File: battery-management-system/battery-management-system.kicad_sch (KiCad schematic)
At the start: 0 parts

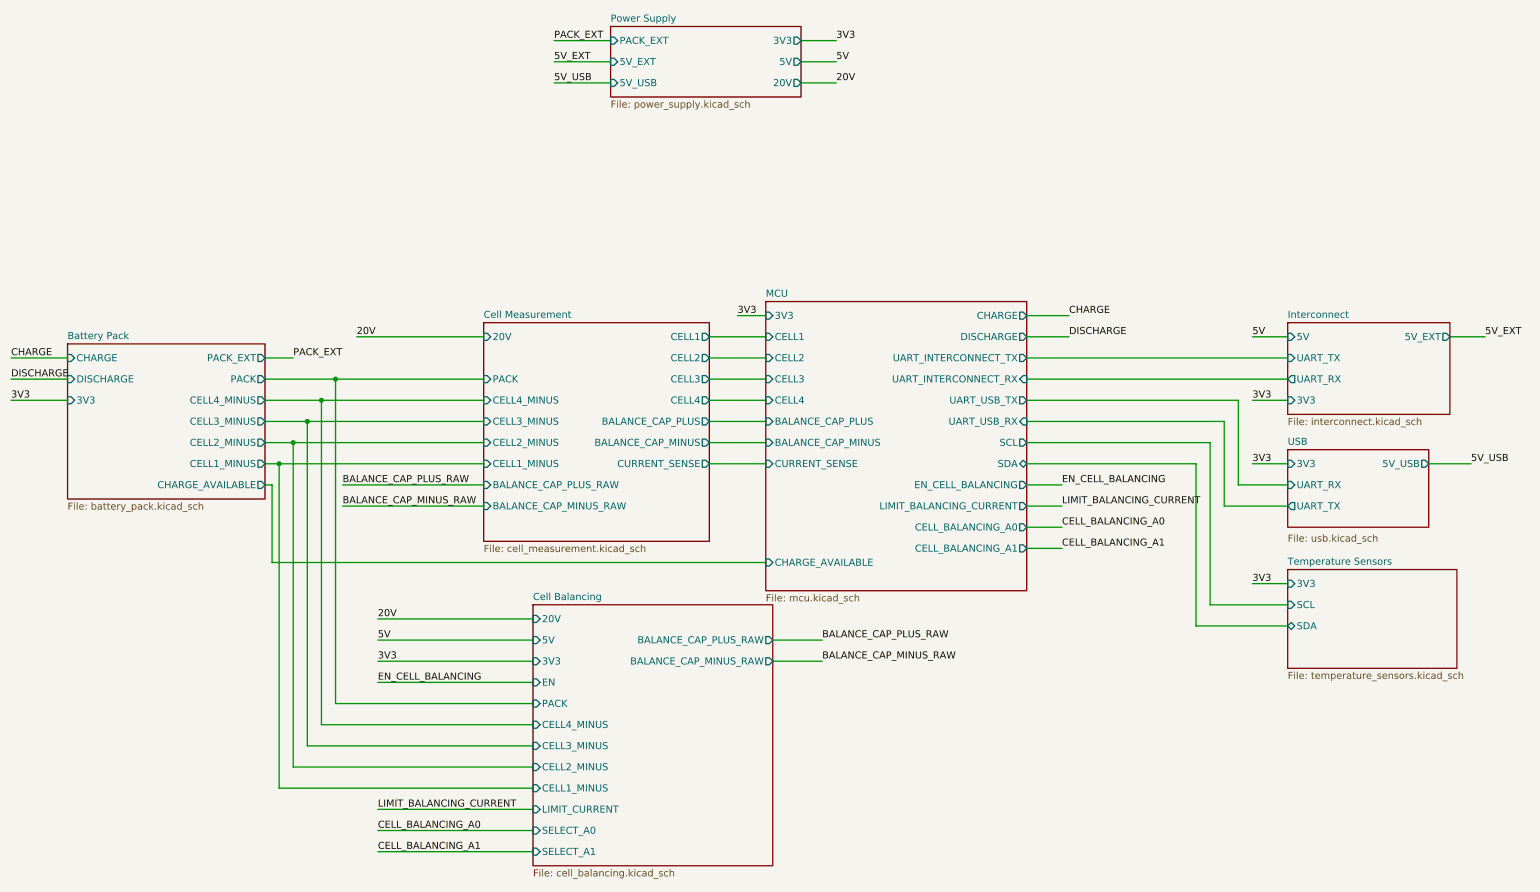
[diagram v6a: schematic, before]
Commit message: add negative power supply for OPAMPs
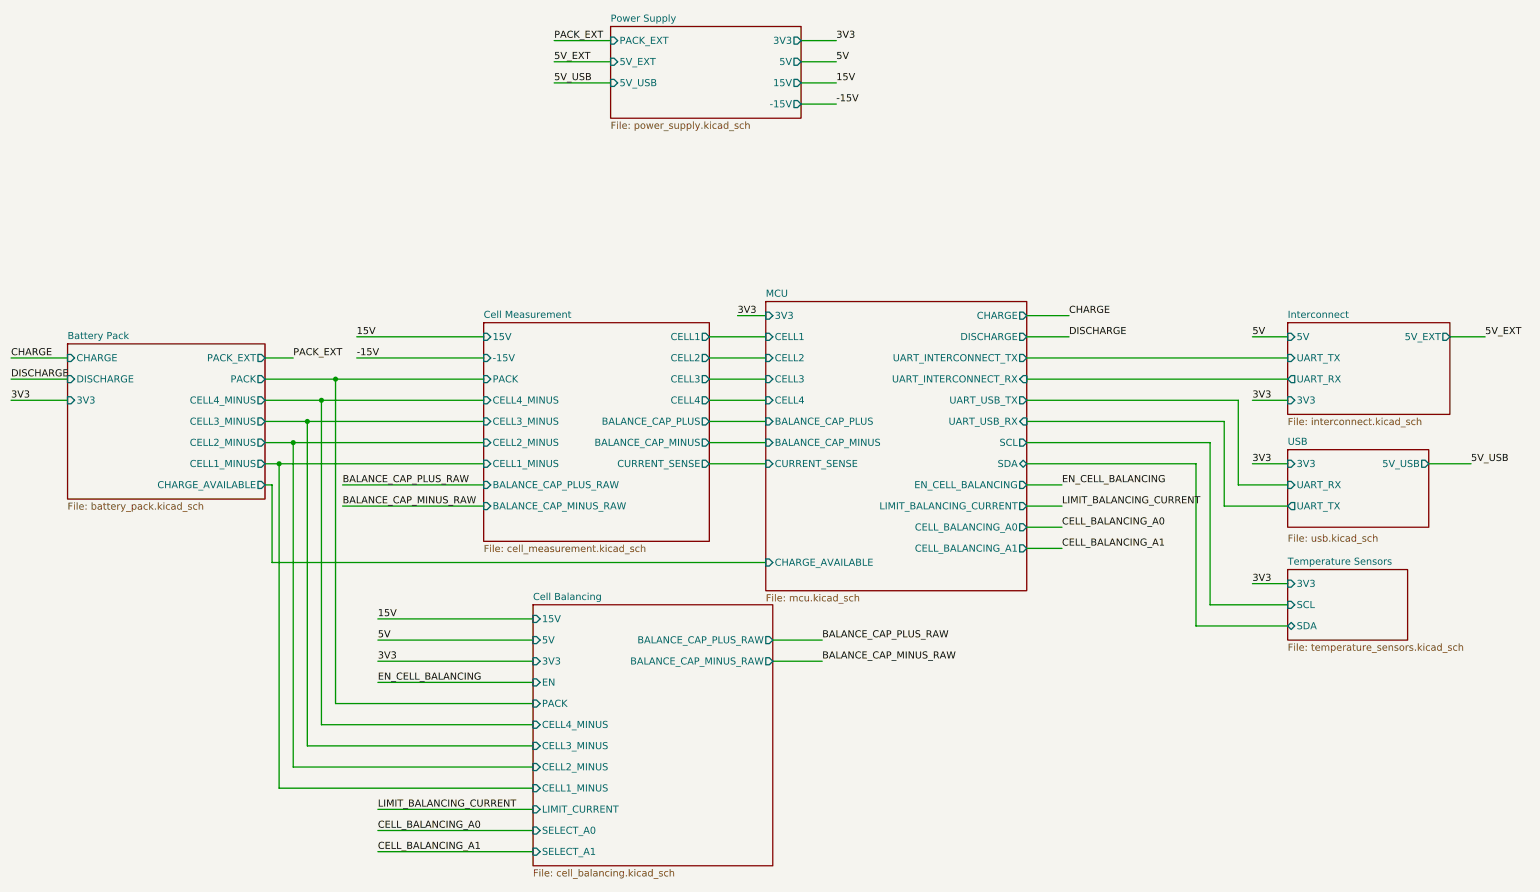
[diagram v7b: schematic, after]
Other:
- sheet Cell Balancing ports: added 15V; removed 20V
- sheet Cell Measurement ports: added -15V, 15V; removed 20V
- sheet Power Supply ports: added -15V, 15V; removed 20V
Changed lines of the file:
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@@
+    (stroke (width 0) (type default))
+  )
+  (wire (pts (xy 154.94 38.1) (xy 161.29 38.1))
     (stroke (width 0) (type default))
   )
@@
     (stroke (width 0) (type default))
   )
+  (wire (pts (xy 74.93 83.82) (xy 97.79 83.82))
+    (stroke (width 0) (type default))
+  )
   (wire (pts (xy 63.5 99.06) (xy 97.79 99.06))
     (stroke (width 0) (type default))
@@
     (stroke (width 0) (type default))
   )
-  (label "20V" (at 161.29 34.29 0) (fields_autoplaced)
-    (effects (font (size 1.27 1.27)) (justify left bottom))
-  )
-  (label "20V" (at 74.93 80.01 0) (fields_autoplaced)
+  (label "15V" (at 161.29 34.29 0) (fields_autoplaced)
+    (effects (font (size 1.27 1.27)) (justify left bottom))
+  )
+  (label "15V" (at 74.93 80.01 0) (fields_autoplaced)
     (effects (font (size 1.27 1.27)) (justify left bottom))
   )
@@
     (effects (font (size 1.27 1.27)) (justify left bottom))
   )
+  (label "-15V" (at 74.93 83.82 0) (fields_autoplaced)
+    (effects (font (size 1.27 1.27)) (justify left bottom))
+  )
   (label "CHARGE" (at 12.7 83.82 0) (fields_autoplaced)
     (effects (font (size 1.27 1.27)) (justify left bottom))
@@
     (effects (font (size 1.27 1.27)) (justify left bottom))
   )
+  (label "-15V" (at 161.29 38.1 0) (fields_autoplaced)
+    (effects (font (size 1.27 1.27)) (justify left bottom))
+  )
   (label "EN_CELL_BALANCING" (at 78.74 142.24 0) (fields_autoplaced)
     (effects (font (size 1.27 1.27)) (justify left bottom))
@@
     (effects (font (size 1.27 1.27)) (justify left bottom))
   )
-  (label "20V" (at 78.74 130.81 0) (fields_autoplaced)
+  (label "15V" (at 78.74 130.81 0) (fields_autoplaced)
     (effects (font (size 1.27 1.27)) (justify left bottom))
   )
@@
     )
   )
-  (sheet (at 242.57 121.92) (size 30.48 17.78) (fields_autoplaced)
+  (sheet (at 242.57 121.92) (size 21.59 12.7) (fields_autoplaced)
     (stroke (width 0.1524) (type solid))
     (fill (color 0 0 0 0.0000))
@@
       (effects (font (size 1.27 1.27)) (justify left bottom))
     )
-    (property "Sheetfile" "temperature_sensors.kicad_sch" (at 242.57 140.2846 0)
+    (property "Sheetfile" "temperature_sensors.kicad_sch" (at 242.57 135.2046 0)
       (effects (font (size 1.27 1.27)) (justify left top))
     )
@@
       (effects (font (size 1.27 1.27)) (justify left))
     )
-    (pin "20V" input (at 106.68 130.81 180)
-      (effects (font (size 1.27 1.27)) (justify left))
-    )
     (pin "3V3" input (at 106.68 138.43 180)
       (effects (font (size 1.27 1.27)) (justify left))
     )
     (pin "5V" input (at 106.68 134.62 180)
+      (effects (font (size 1.27 1.27)) (justify left))
+    )
+    (pin "15V" input (at 106.68 130.81 180)
       (effects (font (size 1.27 1.27)) (justify left))
     )
@@
       (effects (font (size 1.27 1.27)) (justify left))
     )
-    (pin "20V" input (at 97.79 80.01 180)
-      (effects (font (size 1.27 1.27)) (justify left))
-    )
     (pin "CELL1" output (at 138.43 80.01 0)
       (effects (font (size 1.27 1.27)) (justify right))
@@
     )
     (pin "CELL1_MINUS" input (at 97.79 102.87 180)
+      (effects (font (size 1.27 1.27)) (justify left))
+    )
+    (pin "-15V" input (at 97.79 83.82 180)
+      (effects (font (size 1.27 1.27)) (justify left))
+    )
+    (pin "15V" input (at 97.79 80.01 180)
       (effects (font (size 1.27 1.27)) (justify left))
     )
@@
     )
   )
-  (sheet (at 120.65 24.13) (size 34.29 12.7) (fields_autoplaced)
+  (sheet (at 120.65 24.13) (size 34.29 16.51) (fields_autoplaced)
     (stroke (width 0.1524) (type solid))
     (fill (color 0 0 0 0.0000))
@@
       (effects (font (size 1.27 1.27)) (justify left bottom))
     )
-    (property "Sheetfile" "power_supply.kicad_sch" (at 120.65 37.4146 0)
+    (property "Sheetfile" "power_supply.kicad_sch" (at 120.65 41.2246 0)
       (effects (font (size 1.27 1.27)) (justify left top))
     )
@@
       (effects (font (size 1.27 1.27)) (justify left))
     )
-    (pin "20V" output (at 154.94 34.29 0)
-      (effects (font (size 1.27 1.27)) (justify right))
-    )
+    (pin "15V" output (at 154.94 34.29 0)
+      (effects (font (size 1.27 1.27)) (justify right))
+    )
+    (pin "-15V" output (at 154.94 38.1 0)
+      (effects (font (size 1.27 1.27)) (justify right))
+    )

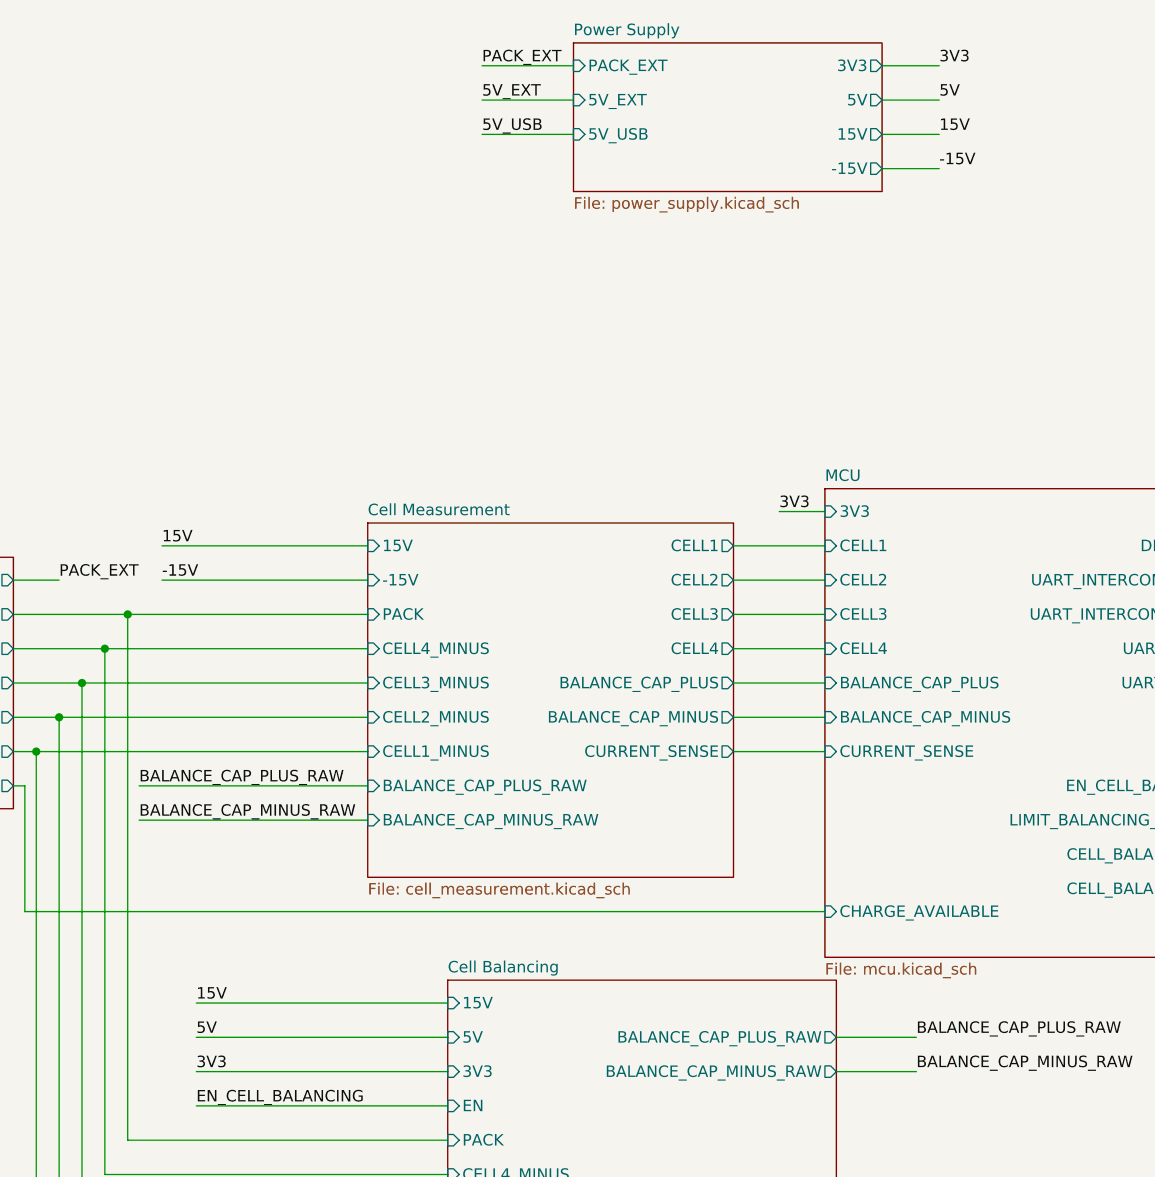
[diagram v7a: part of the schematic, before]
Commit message: implement negative power supply for OPAMPs
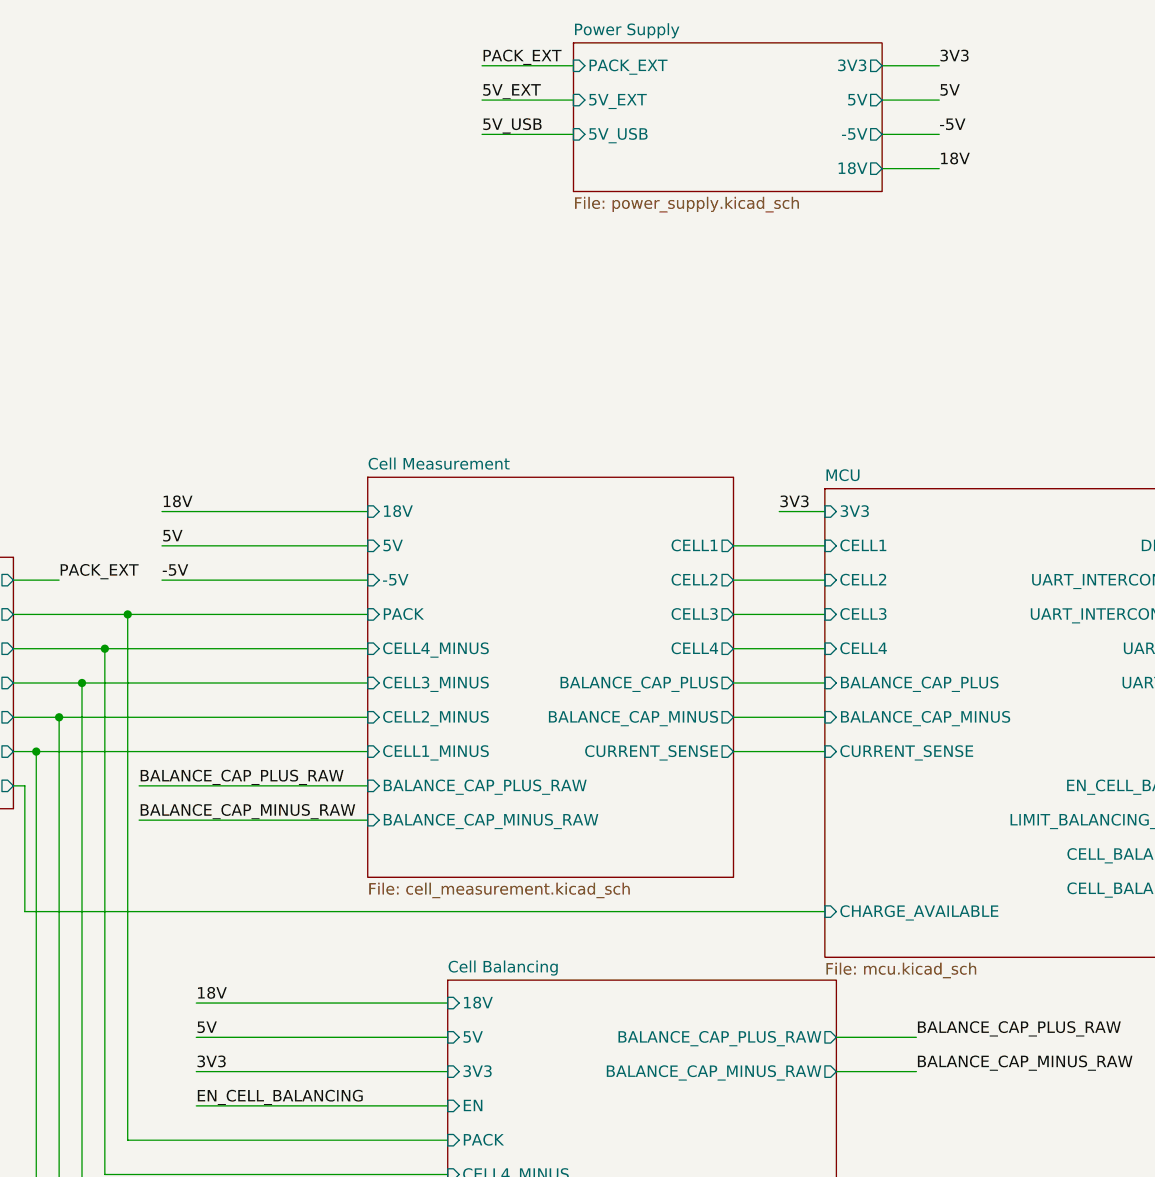
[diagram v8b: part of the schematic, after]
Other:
- sheet Cell Balancing ports: added 18V; removed 15V
- sheet Cell Measurement ports: added -5V, 18V, 5V; removed -15V, 15V
- sheet Power Supply ports: added -5V, 18V; removed -15V, 15V
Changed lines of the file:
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@@
+    (stroke (width 0) (type default))
+  )
+  (wire (pts (xy 12.7 91.44) (xy 22.86 91.44))
+    (stroke (width 0) (type default))
+  )
+  (wire (pts (xy 71.12 87.63) (xy 97.79 87.63))
+    (stroke (width 0) (type default))
+  )
+  (wire (pts (xy 154.94 34.29) (xy 161.29 34.29))
+    (stroke (width 0) (type default))
+  )
+  (wire (pts (xy 236.22 102.87) (xy 242.57 102.87))
+    (stroke (width 0) (type default))
+  )
+  (wire (pts (xy 60.96 102.87) (xy 58.42 102.87))
+    (stroke (width 0) (type default))
+  )
+  (wire (pts (xy 110.49 34.29) (xy 120.65 34.29))
+    (stroke (width 0) (type default))
+  )
+  (wire (pts (xy 231.14 110.49) (xy 242.57 110.49))
+    (stroke (width 0) (type default))
+  )
+  (wire (pts (xy 195.58 106.68) (xy 201.93 106.68))
+    (stroke (width 0) (type default))
+  )
+  (wire (pts (xy 60.96 102.87) (xy 60.96 161.29))
+    (stroke (width 0) (type default))
+  )
+  (wire (pts (xy 59.69 120.65) (xy 59.69 106.68))
     (stroke (width 0) (type default))
   )
@@
     (stroke (width 0) (type default))
   )
-  (wire (pts (xy 12.7 91.44) (xy 22.86 91.44))
-    (stroke (width 0) (type default))
-  )
-  (wire (pts (xy 71.12 87.63) (xy 97.79 87.63))
-    (stroke (width 0) (type default))
-  )
-  (wire (pts (xy 236.22 102.87) (xy 242.57 102.87))
-    (stroke (width 0) (type default))
-  )
-  (wire (pts (xy 60.96 102.87) (xy 58.42 102.87))
-    (stroke (width 0) (type default))
-  )
-  (wire (pts (xy 110.49 34.29) (xy 120.65 34.29))
-    (stroke (width 0) (type default))
-  )
-  (wire (pts (xy 231.14 110.49) (xy 242.57 110.49))
-    (stroke (width 0) (type default))
-  )
-  (wire (pts (xy 195.58 106.68) (xy 201.93 106.68))
-    (stroke (width 0) (type default))
-  )
-  (wire (pts (xy 60.96 102.87) (xy 60.96 161.29))
-    (stroke (width 0) (type default))
-  )
-  (wire (pts (xy 59.69 120.65) (xy 59.69 106.68))
-    (stroke (width 0) (type default))
-  )
-  (wire (pts (xy 154.94 34.29) (xy 161.29 34.29))
-    (stroke (width 0) (type default))
-  )
   (wire (pts (xy 78.74 138.43) (xy 106.68 138.43))
     (stroke (width 0) (type default))
@@
     (stroke (width 0) (type default))
   )
+  (wire (pts (xy 74.93 76.2) (xy 97.79 76.2))
+    (stroke (width 0) (type default))
+  )
   (wire (pts (xy 226.06 132.08) (xy 242.57 132.08))
     (stroke (width 0) (type default))
@@
     (stroke (width 0) (type default))
   )
-  (label "15V" (at 161.29 34.29 0) (fields_autoplaced)
-    (effects (font (size 1.27 1.27)) (justify left bottom))
-  )
-  (label "15V" (at 74.93 80.01 0) (fields_autoplaced)
+  (label "18V" (at 161.29 38.1 0) (fields_autoplaced)
+    (effects (font (size 1.27 1.27)) (justify left bottom))
+  )
+  (label "5V" (at 74.93 80.01 0) (fields_autoplaced)
     (effects (font (size 1.27 1.27)) (justify left bottom))
   )
@@
     (effects (font (size 1.27 1.27)) (justify left bottom))
   )
-  (label "-15V" (at 74.93 83.82 0) (fields_autoplaced)
+  (label "-5V" (at 74.93 83.82 0) (fields_autoplaced)
     (effects (font (size 1.27 1.27)) (justify left bottom))
   )
@@
     (effects (font (size 1.27 1.27)) (justify left bottom))
   )
-  (label "-15V" (at 161.29 38.1 0) (fields_autoplaced)
+  (label "-5V" (at 161.29 34.29 0) (fields_autoplaced)
     (effects (font (size 1.27 1.27)) (justify left bottom))
   )
@@
     (effects (font (size 1.27 1.27)) (justify left bottom))
   )
-  (label "15V" (at 78.74 130.81 0) (fields_autoplaced)
+  (label "18V" (at 78.74 130.81 0) (fields_autoplaced)
     (effects (font (size 1.27 1.27)) (justify left bottom))
   )
@@
   )
   (label "5V_EXT" (at 110.49 30.48 0) (fields_autoplaced)
+    (effects (font (size 1.27 1.27)) (justify left bottom))
+  )
+  (label "18V" (at 74.93 76.2 0) (fields_autoplaced)
     (effects (font (size 1.27 1.27)) (justify left bottom))
   )
@@
       (effects (font (size 1.27 1.27)) (justify left))
     )
-    (pin "15V" input (at 106.68 130.81 180)
+    (pin "18V" input (at 106.68 130.81 180)
       (effects (font (size 1.27 1.27)) (justify left))
     )
@@
     )
   )
-  (sheet (at 97.79 77.47) (size 40.64 39.37) (fields_autoplaced)
+  (sheet (at 97.79 72.39) (size 40.64 44.45) (fields_autoplaced)
     (stroke (width 0.1524) (type solid))
     (fill (color 0 0 0 0.0000))
-    (property "Sheetname" "Cell Measurement" (at 97.79 76.7584 0)
+    (property "Sheetname" "Cell Measurement" (at 97.79 71.6784 0)
       (effects (font (size 1.27 1.27)) (justify left bottom))
     )
@@
       (effects (font (size 1.27 1.27)) (justify left))
     )
-    (pin "-15V" input (at 97.79 83.82 180)
-      (effects (font (size 1.27 1.27)) (justify left))
-    )
-    (pin "15V" input (at 97.79 80.01 180)
+    (pin "-5V" input (at 97.79 83.82 180)
+      (effects (font (size 1.27 1.27)) (justify left))
+    )
+    (pin "5V" input (at 97.79 80.01 180)
+      (effects (font (size 1.27 1.27)) (justify left))
+    )
+    (pin "18V" input (at 97.79 76.2 180)
       (effects (font (size 1.27 1.27)) (justify left))
     )
@@
       (effects (font (size 1.27 1.27)) (justify left))
     )
-    (pin "15V" output (at 154.94 34.29 0)
-      (effects (font (size 1.27 1.27)) (justify right))
-    )
-    (pin "-15V" output (at 154.94 38.1 0)
-      (effects (font (size 1.27 1.27)) (justify right))
-    )
+    (pin "-5V" output (at 154.94 34.29 0)
+      (effects (font (size 1.27 1.27)) (justify right))
+    )
+    (pin "18V" output (at 154.94 38.1 0)
+      (effects (font (size 1.27 1.27)) (justify right))
+    )
